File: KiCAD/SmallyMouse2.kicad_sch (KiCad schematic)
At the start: 34 parts, among them IC1 AT90USB1287, J1 Exp Header, J2 Slow/Fast, J3 BBC_UP_02X10, J4 Universal output, J5 Bootloader, J6 Reset, P1 USB_A, Y1 16 MHz Crystal

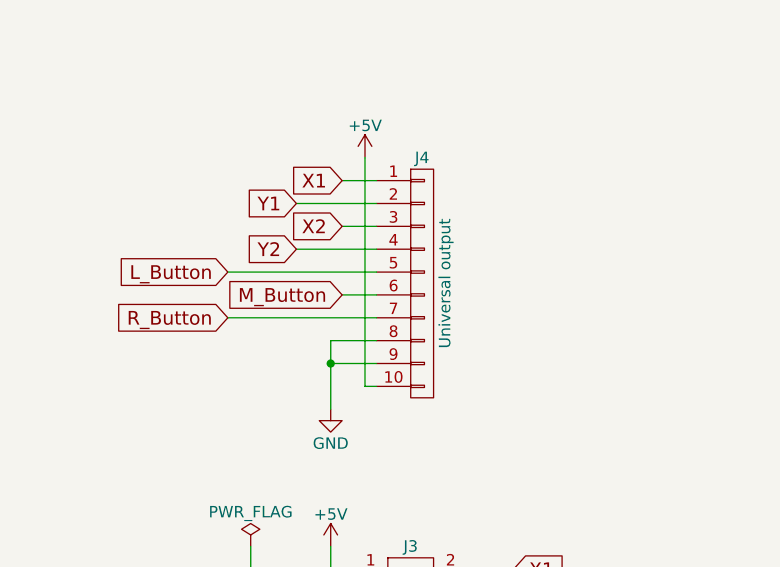
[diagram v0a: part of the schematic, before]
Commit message: Add Manufacturer/MPN for most parts (HKC crystal not on Digikey, so found an NDK equivalent - 2-SMD 5x3.2mm, 8pF, 50Ω)
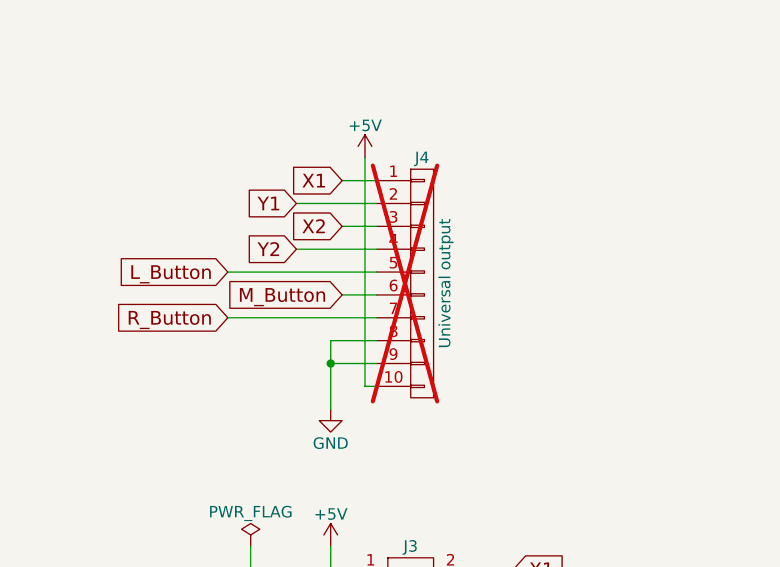
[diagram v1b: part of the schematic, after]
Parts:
- C1, C2: MPN (none) -> GCM21A5C2E220JX01D; Manufacturer (none) -> Murata Electronics
- C10, C3, C5, C6, C7, C8, C9: MPN (none) -> GCM21BR72A104KA37L; Manufacturer (none) -> Murata Electronics
- C4: MPN (none) -> GRM21BR71A105MA01L; Manufacturer (none) -> Murata Electronics
- IC1: MPN (none) -> AT90USB1287-AU; Manufacturer (none) -> Microchip Technology
- J3: MPN (none) -> SBH11-PBPC-D10-ST-BK; Manufacturer (none) -> Sullins Connector Solutions
- J4: now not fitted; now left out of the parts list
- P1: MPN (none) -> 87583-2010BLF; Manufacturer (none) -> Amphenol ICC (FCI)
- R1, R2: MPN (none) -> RMCF0805FT22R0; Manufacturer (none) -> Stackpole Electronics Inc
- R3, R4: MPN (none) -> RMCF0805FT10K0; Manufacturer (none) -> Stackpole Electronics Inc
- Y1: MPN (none) -> STDCSK4-16M; Manufacturer (none) -> NDK (NIHON DEMPA KOGYO CO., LTD)
